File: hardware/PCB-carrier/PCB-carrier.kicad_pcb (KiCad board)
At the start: 4 copper layers, 24 x 115.7 mm, 18 parts

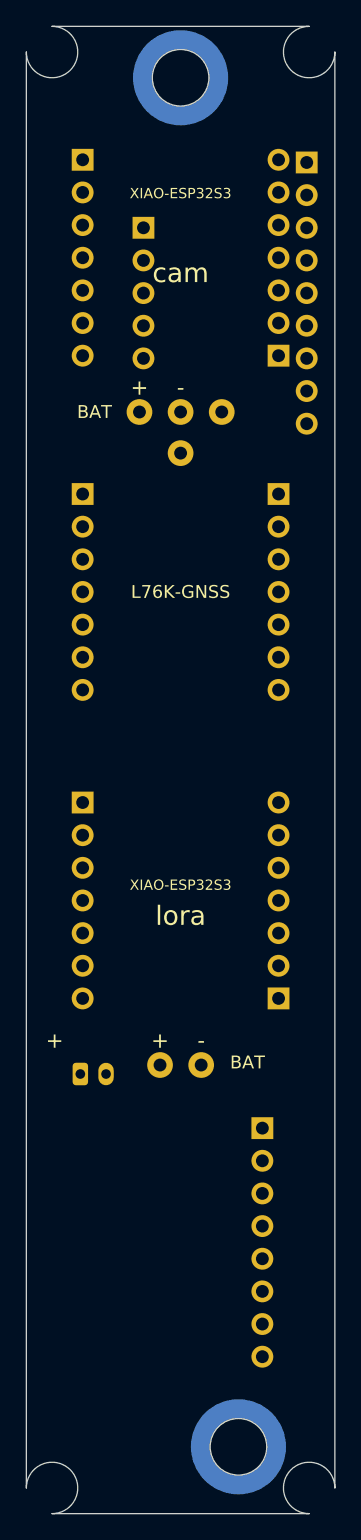
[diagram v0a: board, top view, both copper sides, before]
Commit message: feat(carrier): turn XIAO-ESP32S3-lora 90 deg; draw the two data-link jumpers
- XIAO-ESP32S3-lora turned 90 deg, USB-C out the long edge on the JST's
  side, so its BAT pads face forward toward its pigtail holes. Its rows now
  lie across the board; verify_pins() checks them from the photo turned by
  hand, and the Seeed-row check measures them along y.
- The two data links (GPS -> cam, cam -> lora): each a 2-pin header and a
  1 kOhm lying flat, at the tall side's forward end, nose z 116-129.
  GPS link pin 1 is on GPS_RX. The far ends are not netted: which XIAO
  pins they meet is still owed (#26).
- BMP388 back-silk label moved between the links' holes (DRC).
- Diagram and template label the turned lora's pins upright beside its
  rows; template callouts for the links, re-spaced.
- Regenerated: board, layout JSON/SVG, fit mock STL and holes, template.
  verify: 80 through-holes clear. DRC: 0 violations, 13 unconnected
  (the unrouted nets).

Refs #34, #26

Co-Authored-By: Claude Opus 5.5 <noreply@anthropic.com>
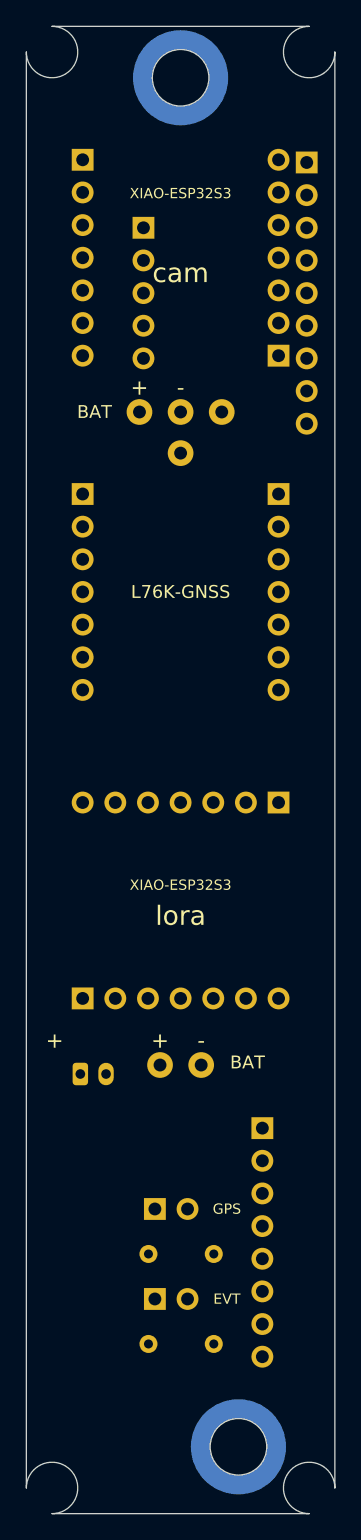
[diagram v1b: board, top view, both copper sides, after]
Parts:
- added J_LINK_EVT: PinHeader_1x02_P2.54mm_Vertical, PinHeader_1x02_P2.54mm_Vertical, F.Cu at (10.0, 99.0)
- added J_LINK_GPS: PinHeader_1x02_P2.54mm_Vertical, PinHeader_1x02_P2.54mm_Vertical, F.Cu at (10.0, 92.0)
- added R_LINK_EVT: R_Axial_DIN0204_L3.6mm_D1.6mm_P5.08mm_Horizontal, R_Axial_DIN0204_L3.6mm_D1.6mm_P5.08mm_Horizontal, F.Cu at (9.50, 102.5)
- added R_LINK_GPS: R_Axial_DIN0204_L3.6mm_D1.6mm_P5.08mm_Horizontal, R_Axial_DIN0204_L3.6mm_D1.6mm_P5.08mm_Horizontal, F.Cu at (9.50, 95.5)
- moved J_LORA_A 15.2 mm to (4.38, 75.6), turned to 90 degrees
- moved J_LORA_B 15.2 mm to (19.6, 60.4), turned to -90 degrees
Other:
- board text added: "EVT"
- board text added: "GPS"

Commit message: feat(carrier): battery off the board -- Y-cable harness; pigtail holes are anchors
Operator, 2026-10-11, at the first fit of the printed sled and mock: a
Y-cable joins the battery to both XIAOs' pigtails, and the battery's
lead runs aft to below the sled, where it unplugs for the charger.

- gen_carrier.py: J_BAT (JST-PH) and the VBAT net removed. The four
  pigtail holes stay where they were, unnetted: the wires lace through
  them as strain relief. 78 through-holes clear; DRC 0 violations, 11
  unconnected (the unrouted nets).
- Template callouts and note: anchors, laced through, not soldered.
- Regenerated: board, layout, diagram, template, fit mock (80 holes,
  proven open on every layer of the PLA slice).
- Docs: PCB-carrier, PCB-carrier-design, LiPo-500mAh (the bench join
  harness is now the flight harness), design.md, README, Arming-switch.

Refs #30

Co-Authored-By: Claude Opus 5.5 <noreply@anthropic.com>
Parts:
- removed J_BAT: JST_PH_S2B-PH-K_1x02_P2.00mm_Horizontal, JST_PH_S2B-PH-K_1x02_P2.00mm_Horizontal
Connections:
- TP_CAM_BAT_N pad 1: GND -> (no net)
- TP_CAM_BAT_P pad 1: VBAT -> (no net)
- TP_LORA_BAT_N pad 1: GND -> (no net)
- TP_LORA_BAT_P pad 1: VBAT -> (no net)

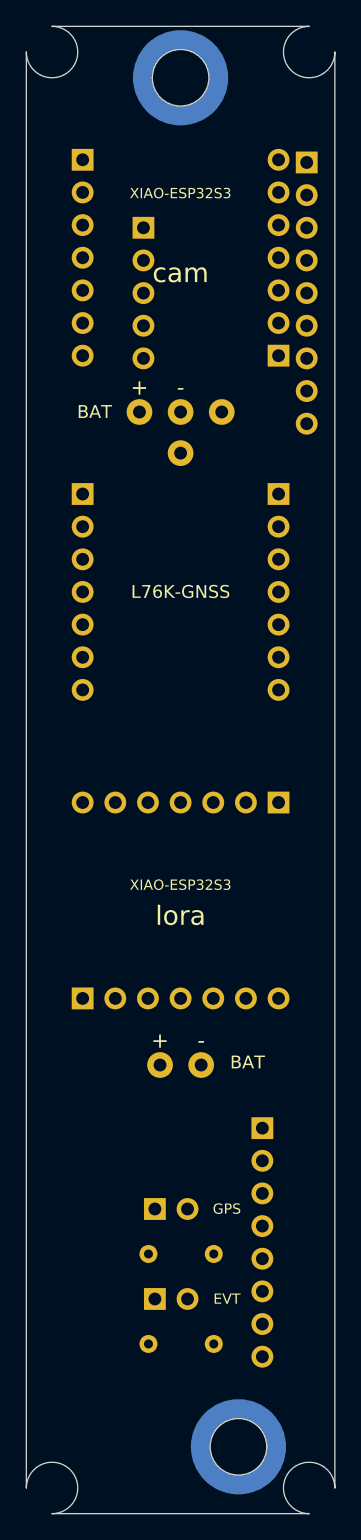
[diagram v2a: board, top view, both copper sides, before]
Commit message: feat(carrier): PS1240 on the board, BMP388 turned on spacers, data links to the edges
The buzzer had no mount: on the BOM since August, wire pads on the carrier
since September, and never placed. It now sits on the tall side at the forward
end (board 11.5, 103.0 = nose z 128.4), facing a sound hole in the Nosecone.

To make room, the BMP388 is turned 90 deg on the low side (row across the
board, aft) and held by spacers through its own holes -- no bolt and no carrier
hole -- and the two data-link jumpers move to the board's edges just forward of
the lora XIAO's battery anchors. The cam XIAO, L76K-GNSS and lora XIAO do not
move, so the LoRa antenna lead is unaffected.

verify_pins/verify_clearances pass (78 through-holes, new PS1240 keep-out);
DRC 0 violations, 11 unconnected (unrouted, unchanged). Fit mock regenerated,
arrow moved clear of the disc; all 84 holes verified open in the G-code.
Buzzer lead pitch 5.0 mm is TDK's catalog value: caliper the part before ordering.

Refs #36

Co-Authored-By: Claude Opus 5.5 <noreply@anthropic.com>
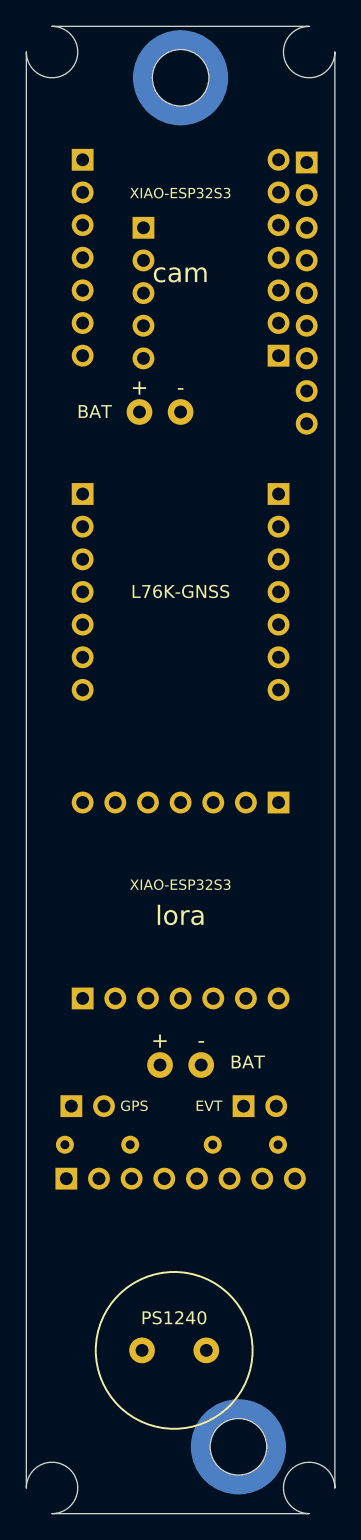
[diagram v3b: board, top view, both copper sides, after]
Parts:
- moved TP_BUZ 73.3 mm to (9.00, 103.0)
- moved TP_BUZ_G 69.8 mm to (14.0, 103.0)
- moved J_LINK_EVT 16.5 mm to (16.9, 84.0)
- moved R_LINK_EVT 16.3 mm to (14.5, 87.0)
- moved J_BMP 15.7 mm to (3.11, 89.6), turned to -90 degrees
- moved R_LINK_GPS 10.7 mm to (3.00, 87.0)
- moved J_LINK_GPS 10.3 mm to (3.50, 84.0)
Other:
- board text added: "PS1240"

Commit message: feat(carrier): lora XIAO next to the cam XIAO, L76K-GNSS turned and forward of it
Operator, 2026-10-15/16. XIAO-ESP32S3-lora moves from LORA_Y 68.0 to 41.4
(nose z 57.9-75.7), about 27 mm nearer the LoRa strip at the PORT end, whose
lead was too short. The L76K-GNSS is turned 90 deg -- rows across the board,
antenna end toward +x, away from the edge the LoRa lead runs round -- and sits
forward of the lora's battery anchors (nose z 82.1-100.1), about 22 mm nearer
its patch. The earlier swap failed only because the GNSS landed on the BMP388,
which has since been turned and moved forward.

verify_pins checks the turned L76K by a second, by-eye route; 78 through-holes
clear; DRC 0 violations, 11 unconnected (unrouted, unchanged). Fit mock
regenerated and re-sliced; all 84 holes verified open in the G-code. Drawing:
the lora's pin names sit inside its rows, and the stale sound-hole note is gone.

Refs #36

Co-Authored-By: Claude Opus 5.5 <noreply@anthropic.com>
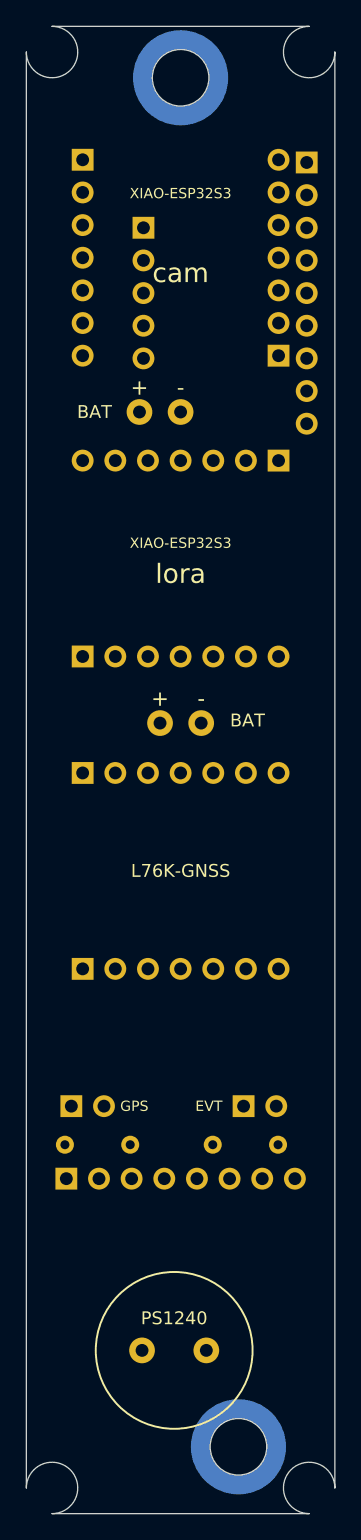
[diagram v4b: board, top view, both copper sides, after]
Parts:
- moved J_L76K_A 36.9 mm to (4.38, 73.3), turned to 90 degrees
- moved J_LORA_A 26.6 mm to (4.38, 49.0)
- moved J_LORA_B 26.6 mm to (19.6, 33.8)
- moved TP_LORA_BAT_N 26.6 mm to (13.6, 54.2)
- moved TP_LORA_BAT_P 26.6 mm to (10.4, 54.2)
- moved J_L76K_B 26.5 mm to (4.38, 58.1), turned to 90 degrees
